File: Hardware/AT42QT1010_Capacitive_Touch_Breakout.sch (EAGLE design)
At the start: 31 parts, among them Q1 600mA/40V, U1 AT42QT1010 - UDFN

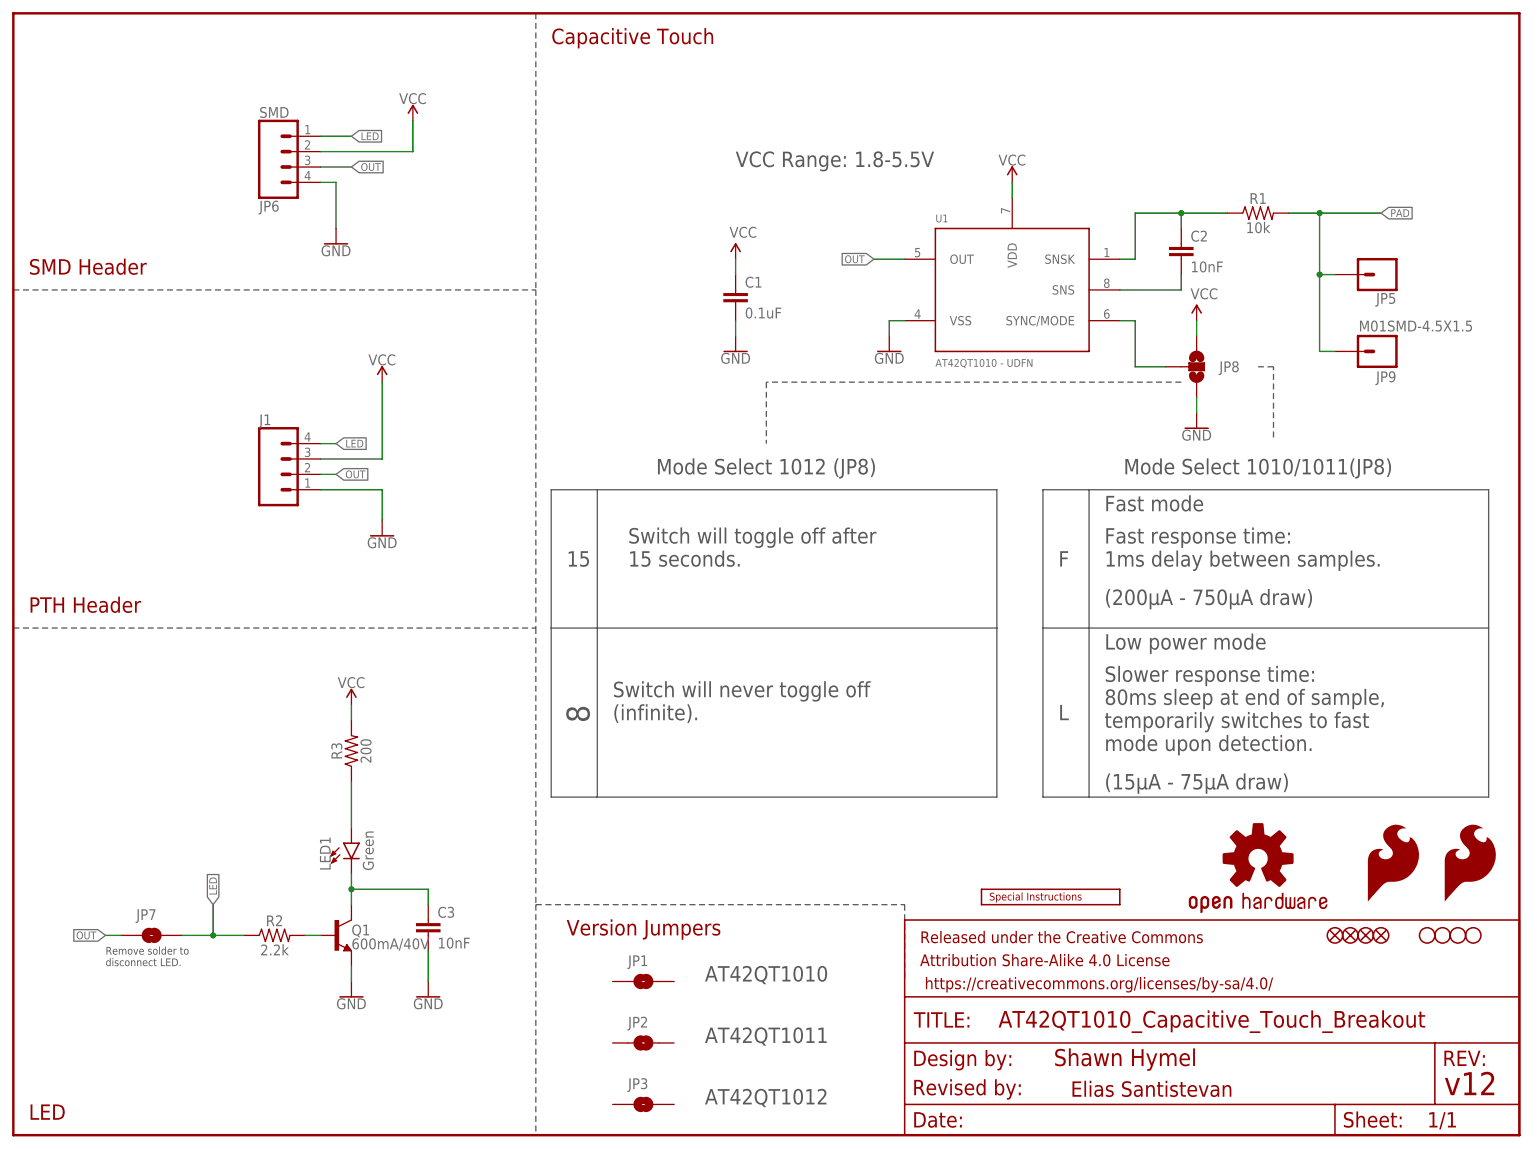
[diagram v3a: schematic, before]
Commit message: Better Labels, replaced jumpers
Much better labels for the selection of low power/fast mode and 15min
timeout vs. no timeout. I also created a device that is a square solder
pad for production to use to identify different versions of the board.
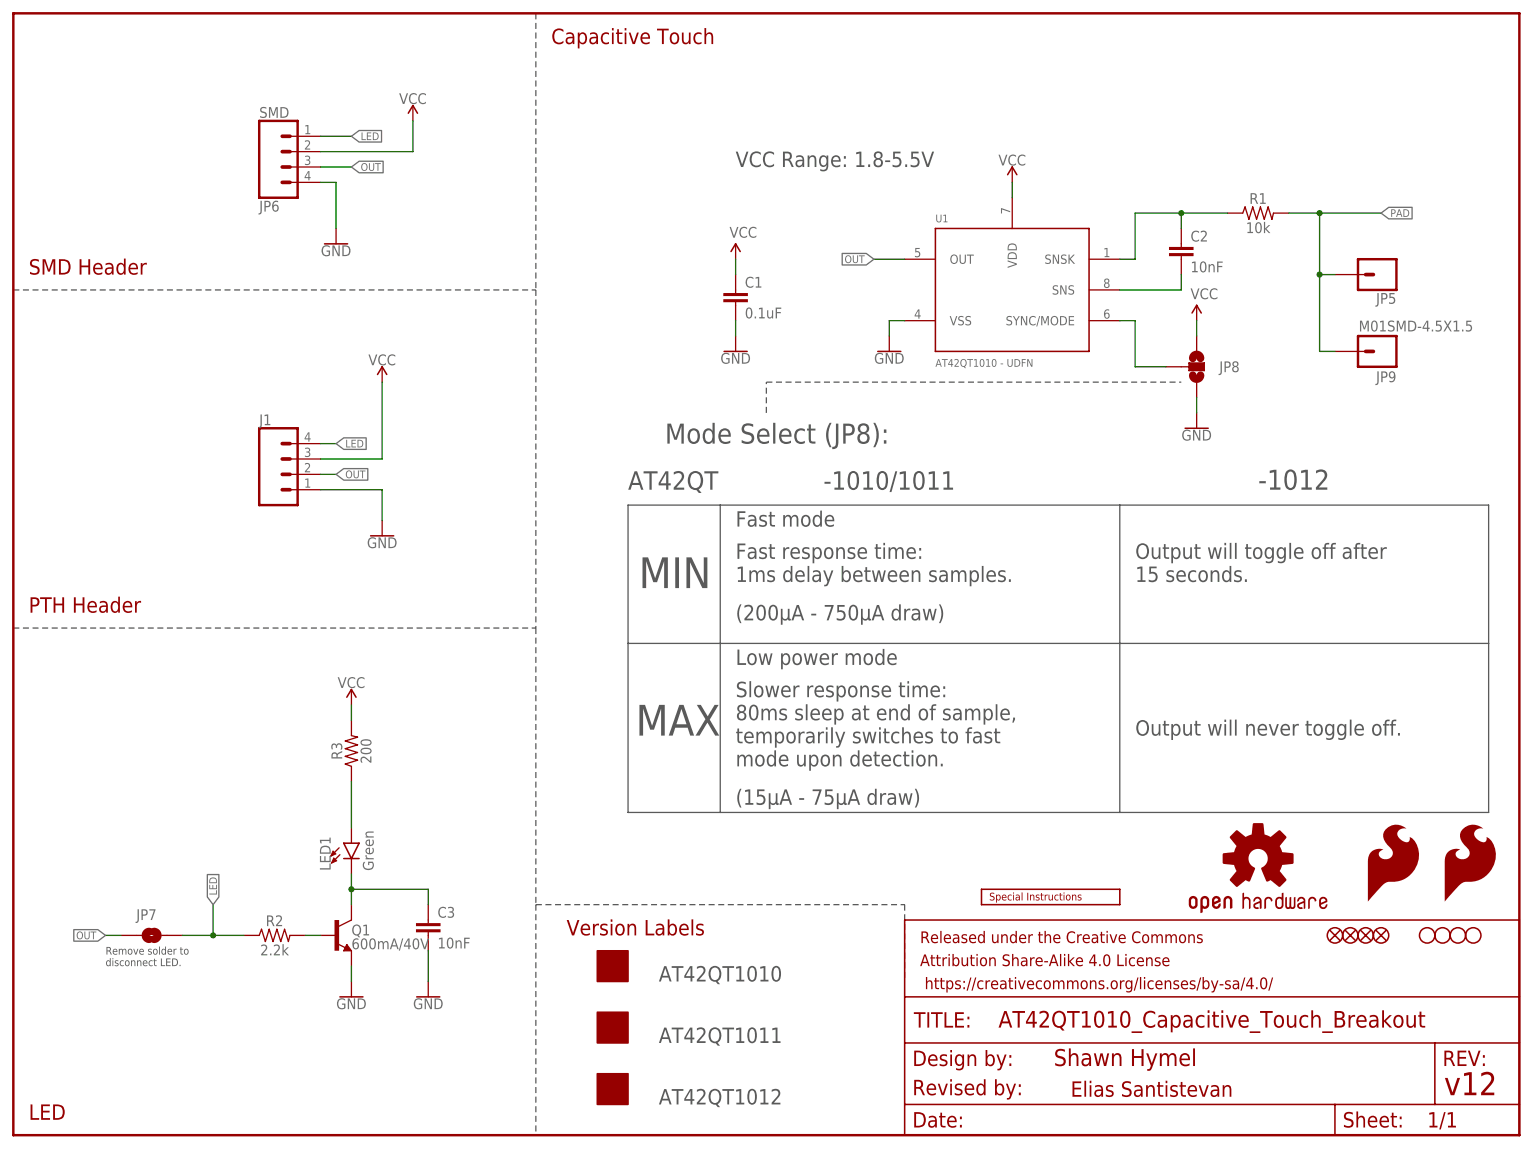
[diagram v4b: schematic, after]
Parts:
- removed JP1, JP2, JP3: JUMPER-SMT_2_NO_SILK, SparkFun-Jumpers:JUMPER-SMT_2_NO_SILK
- added U$2, U$3, U$4: SOLDER_PAD_LABEL, local_parts:SOLDER_PAD_LABEL
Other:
- note added: "-1010/1011"
- note added: "-1012"
- note added: "AT42QT"
- note added: "MAX"
- note added: "MIN"
- note added: "Mode Select (JP8):"
- note added: "Output will never toggle off."
- note added: "Output will toggle off after 15 seconds."
- note added: "Version Labels"
- note removed: "15"
- note removed: "8"
- note removed: "F"
- note removed: "L"
- note removed: "Mode Select 1010/1011(JP8)"
- note removed: "Mode Select 1012 (JP8)"
- note removed: "Switch will never toggle off (infinite)."
- note removed: "Switch will toggle off after 15 seconds."
- note removed: "Version Jumpers"
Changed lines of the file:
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@@
 <part name="U$1" library="SparkFun-Aesthetics" deviceset="SPECIAL_INSTRUCTIONS" device="-ORDERING"/>
 <part name="J1" library="SparkFun-Connectors" deviceset="CONN_04" device=""/>
-<part name="JP1" library="SparkFun-Jumpers" deviceset="JUMPER-SMT_2_NO" device="_SILK"/>
-<part name="JP2" library="SparkFun-Jumpers" deviceset="JUMPER-SMT_2_NO" device="_SILK"/>
-<part name="JP3" library="SparkFun-Jumpers" deviceset="JUMPER-SMT_2_NO" device="_SILK"/>
 <part name="LOGO4" library="SparkFun-Aesthetics" deviceset="SFE_LOGO_FLAME" device=".2_INCH"/>
 <part name="LOGO1" library="SparkFun-Aesthetics" deviceset="SFE_LOGO_FLAME" device=".2_INCH"/>
+<part name="U$2" library="local_parts" deviceset="SOLDER_PAD_LABEL" device=""/>
+<part name="U$3" library="local_parts" deviceset="SOLDER_PAD_LABEL" device=""/>
+<part name="U$4" library="local_parts" deviceset="SOLDER_PAD_LABEL" device=""/>
 </parts>
 <sheets>
@@
 <text x="2.54" y="86.36" size="2.54" layer="94" font="vector">PTH Header</text>
 <text x="2.54" y="2.54" size="2.54" layer="94" font="vector">LED</text>
-<text x="205.74" y="109.22" size="2.54" layer="97" font="vector" align="bottom-center">Mode Select 1010/1011(JP8)</text>
-<text x="172.72" y="93.98" size="2.54" layer="97" font="vector">F</text>
-<text x="172.72" y="68.58" size="2.54" layer="97" font="vector">L</text>
-<text x="180.34" y="103.124" size="2.54" layer="97" font="vector" ratio="15">Fast mode</text>
-<text x="180.34" y="93.98" size="2.54" layer="97" font="vector">Fast response time:
+<text x="144.78" y="106.68" size="3.048" layer="97" font="vector" align="bottom-center">-1010/1011</text>
+<text x="119.38" y="100.584" size="2.54" layer="97" font="vector" ratio="15">Fast mode</text>
+<text x="119.38" y="91.44" size="2.54" layer="97" font="vector">Fast response time:
 1ms delay between samples.</text>
-<text x="180.34" y="80.264" size="2.54" layer="97" font="vector" ratio="15">Low power mode</text>
-<text x="180.34" y="57.15" size="2.54" layer="97" font="vector">(15µA - 75µA draw)</text>
-<text x="180.34" y="63.5" size="2.54" layer="97" font="vector">Slower response time:
+<text x="119.38" y="77.724" size="2.54" layer="97" font="vector" ratio="15">Low power mode</text>
+<text x="119.38" y="54.61" size="2.54" layer="97" font="vector">(15µA - 75µA draw)</text>
+<text x="119.38" y="60.96" size="2.54" layer="97" font="vector">Slower response time:
 80ms sleep at end of sample,
 temporarily switches to fast
 mode upon detection.</text>
-<text x="180.34" y="87.63" size="2.54" layer="97" font="vector">(200µA - 750µA draw)</text>
-<wire x1="170.18" y1="106.68" x2="177.8" y2="106.68" width="0.1524" layer="97"/>
-<wire x1="177.8" y1="106.68" x2="243.84" y2="106.68" width="0.1524" layer="97"/>
-<wire x1="243.84" y1="106.68" x2="243.84" y2="83.82" width="0.1524" layer="97"/>
-<wire x1="243.84" y1="83.82" x2="243.84" y2="55.88" width="0.1524" layer="97"/>
-<wire x1="243.84" y1="55.88" x2="177.8" y2="55.88" width="0.1524" layer="97"/>
-<wire x1="177.8" y1="55.88" x2="170.18" y2="55.88" width="0.1524" layer="97"/>
-<wire x1="170.18" y1="55.88" x2="170.18" y2="83.82" width="0.1524" layer="97"/>
-<wire x1="170.18" y1="83.82" x2="170.18" y2="106.68" width="0.1524" layer="97"/>
-<wire x1="170.18" y1="83.82" x2="243.84" y2="83.82" width="0.1524" layer="97"/>
-<wire x1="177.8" y1="106.68" x2="177.8" y2="55.88" width="0.1524" layer="97"/>
+<text x="119.38" y="85.09" size="2.54" layer="97" font="vector">(200µA - 750µA draw)</text>
+<wire x1="182.88" y1="104.14" x2="243.84" y2="104.14" width="0.1524" layer="97"/>
+<wire x1="243.84" y1="104.14" x2="243.84" y2="81.28" width="0.1524" layer="97"/>
+<wire x1="243.84" y1="81.28" x2="243.84" y2="53.34" width="0.1524" layer="97"/>
+<wire x1="243.84" y1="53.34" x2="182.88" y2="53.34" width="0.1524" layer="97"/>
 <text x="148.59" y="6.604" size="2.54" layer="94" font="vector">Revised by:</text>
 <text x="174.752" y="6.35" size="2.54" layer="94" font="vector" ratio="10">Elias Santistevan</text>
@@
 <text x="15.24" y="27.94" size="1.27" layer="97" font="vector">Remove solder to
 disconnect LED.</text>
-<wire x1="208.28" y1="115.316" x2="208.28" y2="127" width="0.2032" layer="97" style="shortdash"/>
-<wire x1="208.28" y1="127" x2="205.74" y2="127" width="0.2032" layer="97" style="shortdash"/>
 <wire x1="86.36" y1="38.1" x2="147.32" y2="38.1" width="0.2032" layer="97" style="shortdash"/>
 <wire x1="147.32" y1="38.1" x2="147.32" y2="25.4" width="0.2032" layer="97" style="shortdash"/>
-<text x="91.44" y="33.02" size="2.54" layer="94" font="vector">Version Jumpers</text>
-<text x="114.3" y="25.4" size="2.54" layer="97" font="vector">AT42QT1010</text>
-<text x="114.3" y="15.24" size="2.54" layer="97" font="vector">AT42QT1011</text>
-<text x="114.3" y="5.08" size="2.54" layer="97" font="vector">AT42QT1012</text>
-<text x="91.44" y="93.98" size="2.54" layer="97" font="vector">15</text>
-<text x="91.44" y="71.12" size="3.81" layer="97" rot="R270">8</text>
-<text x="124.46" y="109.22" size="2.54" layer="97" font="vector" align="bottom-center">Mode Select 1012 (JP8)</text>
-<wire x1="88.9" y1="106.68" x2="96.52" y2="106.68" width="0.1524" layer="97"/>
-<wire x1="96.52" y1="106.68" x2="162.56" y2="106.68" width="0.1524" layer="97"/>
-<wire x1="162.56" y1="106.68" x2="162.56" y2="83.82" width="0.1524" layer="97"/>
-<wire x1="162.56" y1="83.82" x2="162.56" y2="55.88" width="0.1524" layer="97"/>
-<wire x1="162.56" y1="55.88" x2="96.52" y2="55.88" width="0.1524" layer="97"/>
-<wire x1="96.52" y1="55.88" x2="88.9" y2="55.88" width="0.1524" layer="97"/>
-<wire x1="88.9" y1="55.88" x2="88.9" y2="83.82" width="0.1524" layer="97"/>
-<wire x1="88.9" y1="83.82" x2="88.9" y2="106.68" width="0.1524" layer="97"/>
-<wire x1="88.9" y1="83.82" x2="162.56" y2="83.82" width="0.1524" layer="97"/>
-<wire x1="96.52" y1="106.68" x2="96.52" y2="55.88" width="0.1524" layer="97"/>
-<wire x1="193.04" y1="124.46" x2="124.46" y2="124.46" width="0.2032" layer="97" style="shortdash"/>
-<wire x1="124.46" y1="124.46" x2="124.46" y2="114.3" width="0.2032" layer="97" style="shortdash"/>
-<text x="101.6" y="93.98" size="2.54" layer="97" font="vector">Switch will toggle off after
+<text x="91.44" y="33.02" size="2.54" layer="94" font="vector">Version Labels</text>
+<text x="106.68" y="25.4" size="2.54" layer="97" font="vector">AT42QT1010</text>
+<text x="106.68" y="15.24" size="2.54" layer="97" font="vector">AT42QT1011</text>
+<text x="106.68" y="5.08" size="2.54" layer="97" font="vector">AT42QT1012</text>
+<text x="126.238" y="114.3" size="3.302" layer="97" font="vector" align="bottom-center">Mode Select (JP8):</text>
+<wire x1="101.6" y1="104.14" x2="116.84" y2="104.14" width="0.1524" layer="97"/>
+<wire x1="116.84" y1="104.14" x2="182.88" y2="104.14" width="0.1524" layer="97"/>
+<wire x1="182.88" y1="104.14" x2="182.88" y2="81.28" width="0.1524" layer="97"/>
+<wire x1="182.88" y1="81.28" x2="182.88" y2="53.34" width="0.1524" layer="97"/>
+<wire x1="182.88" y1="53.34" x2="116.84" y2="53.34" width="0.1524" layer="97"/>
+<wire x1="116.84" y1="53.34" x2="101.6" y2="53.34" width="0.1524" layer="97"/>
+<wire x1="101.6" y1="53.34" x2="101.6" y2="81.28" width="0.1524" layer="97"/>
+<wire x1="101.6" y1="81.28" x2="101.6" y2="104.14" width="0.1524" layer="97"/>
+<wire x1="101.6" y1="81.28" x2="182.88" y2="81.28" width="0.1524" layer="97"/>
+<wire x1="116.84" y1="104.14" x2="116.84" y2="53.34" width="0.1524" layer="97"/>
+<text x="185.42" y="91.44" size="2.54" layer="97" font="vector">Output will toggle off after
 15 seconds.</text>
-<text x="99.06" y="68.58" size="2.54" layer="97" font="vector">Switch will never toggle off
-(infinite).</text>
+<text x="185.42" y="66.04" size="2.54" layer="97" font="vector">Output will never toggle off.</text>
+<wire x1="182.88" y1="81.28" x2="243.84" y2="81.28" width="0.2032" layer="97"/>
+<text x="103.378" y="90.424" size="5.08" layer="97" font="vector" ratio="15">MIN</text>
+<text x="102.87" y="66.04" size="5.08" layer="97" font="vector" ratio="15">MAX</text>
+<text x="205.74" y="106.68" size="3.302" layer="97" font="vector">-1012</text>
+<wire x1="124.46" y1="119.38" x2="124.46" y2="124.46" width="0.2032" layer="97" style="shortdash"/>
+<wire x1="124.46" y1="124.46" x2="193.04" y2="124.46" width="0.2032" layer="97" style="shortdash"/>
+<text x="101.6" y="106.68" size="3.048" layer="97" font="vector">AT42QT </text>
 </plain>
 <instances>
@@
 <instance part="U$1" gate="G$1" x="160.02" y="38.1"/>
 <instance part="J1" gate="G$1" x="45.72" y="109.22"/>
-<instance part="JP1" gate="G$1" x="104.14" y="25.4" smashed="yes">
-<attribute name="NAME" x="101.6" y="27.94" size="1.778" layer="95" font="vector"/>
-</instance>
-<instance part="JP2" gate="G$1" x="104.14" y="15.24" smashed="yes">
-<attribute name="NAME" x="101.6" y="17.78" size="1.778" layer="95" font="vector"/>
-</instance>
-<instance part="JP3" gate="G$1" x="104.14" y="5.08" smashed="yes">
-<attribute name="NAME" x="101.6" y="7.62" size="1.778" layer="95" font="vector"/>
-</instance>
 <instance part="LOGO4" gate="G$1" x="223.52" y="38.1"/>
 <instance part="LOGO1" gate="G$1" x="236.22" y="38.1"/>
+<instance part="U$2" gate="G$1" x="99.06" y="27.94"/>
+<instance part="U$3" gate="G$1" x="99.06" y="17.78"/>
+<instance part="U$4" gate="G$1" x="99.06" y="7.62"/>
 </instances>
 <busses>
